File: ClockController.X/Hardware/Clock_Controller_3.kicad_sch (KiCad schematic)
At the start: 14 parts, among them J1 UJC-VP-3-SMT-TR, Q1 DMG7430LFG-7, U4 AP33772DKZ-13

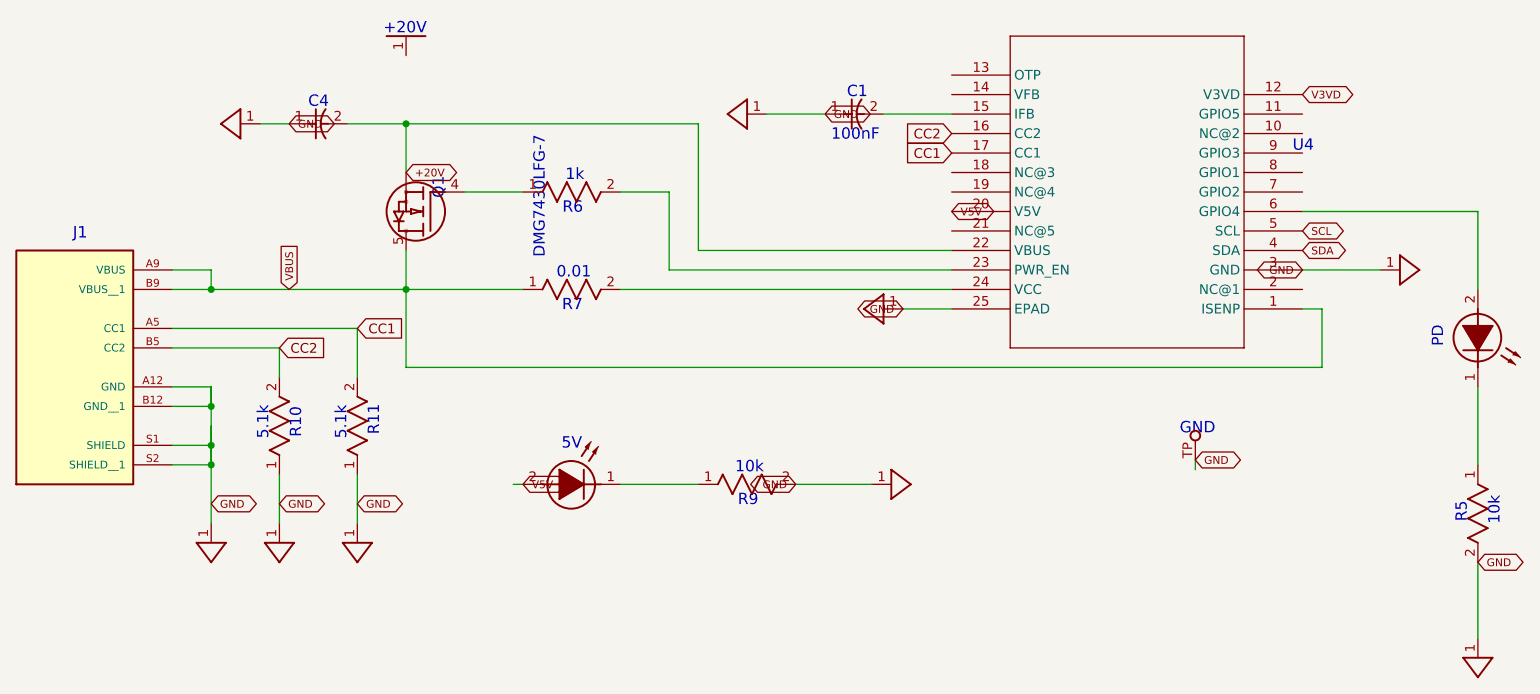
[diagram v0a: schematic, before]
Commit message: Cleaned up a bunch of labels
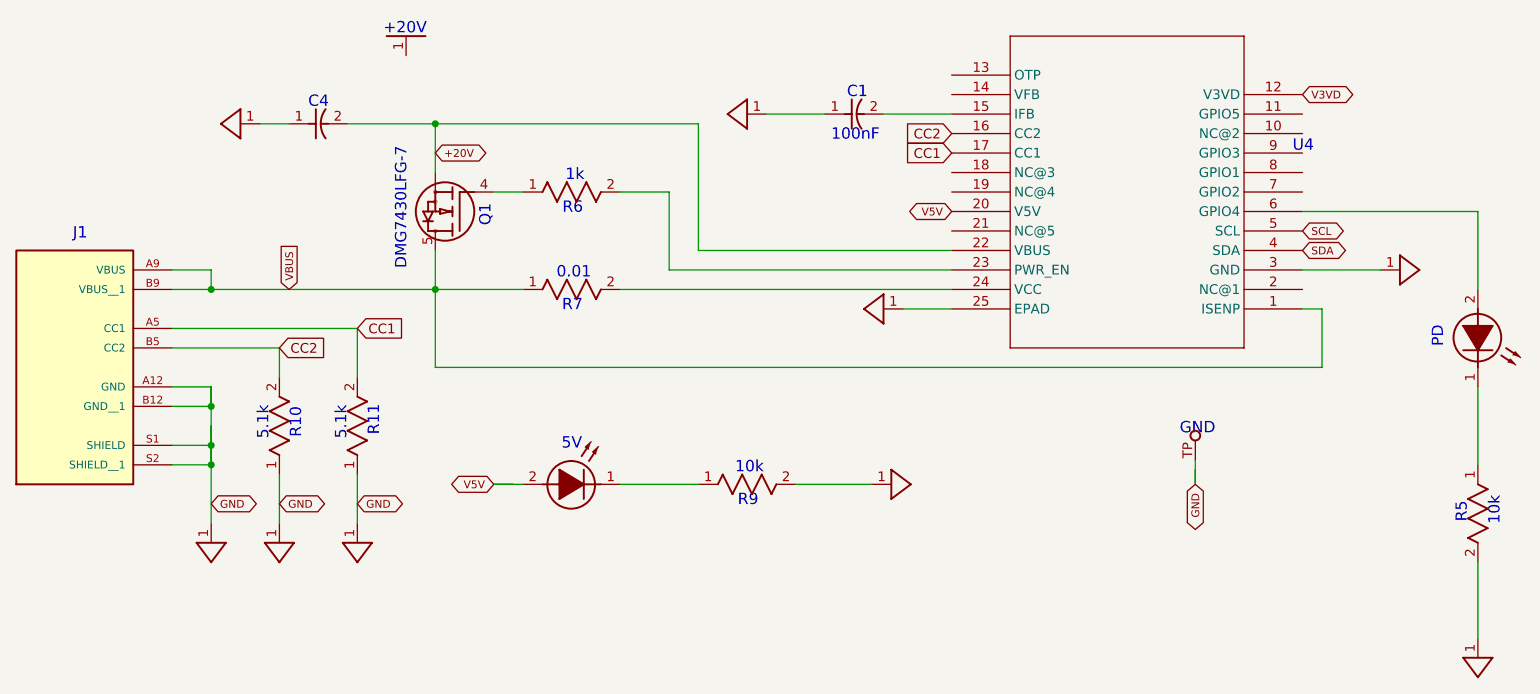
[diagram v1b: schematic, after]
